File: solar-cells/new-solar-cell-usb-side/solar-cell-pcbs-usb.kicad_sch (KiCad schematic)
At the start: 22 parts, among them J1 Solar Cell

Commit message: bottom adapter plate sanity commit
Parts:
- removed H7: MountingHole_Pad, MountingHole:MountingHole_3.2mm_M3_DIN965_Pad, symbol Mechanical:MountingHole_Pad
- renumbered H8 to H7
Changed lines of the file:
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@@
     (pin "2")
-  )
-  (symbol (lib_id "power:GND") (at 48.26 138.43 0) (unit 1)
-    (in_bom yes) (on_board yes) (fields_autoplaced)
-    (property "Reference" "#PWR0108" (id 0) (at 48.26 144.78 0)
-      (effects (font (size 1.27 1.27)) hide)
-    )
-    (property "Value" "GND" (id 1) (at 48.26 143.51 0))
-    (property "Footprint" "" (id 2) (at 48.26 138.43 0)
-      (effects (font (size 1.27 1.27)) hide)
-    )
-    (property "Datasheet" "" (id 3) (at 48.26 138.43 0)
-      (effects (font (size 1.27 1.27)) hide)
-    )
-    (pin "1")
   )
   (symbol (lib_id "power:GND") (at 48.26 121.92 0) (unit 1)
@@
   (symbol (lib_id "Mechanical:MountingHole_Pad") (at 77.47 135.89 0) (unit 1)
     (in_bom yes) (on_board yes) (fields_autoplaced)
-    (property "Reference" "H8" (id 0) (at 80.01 133.3499 0)
+    (property "Reference" "H7" (id 0) (at 80.01 133.3499 0)
       (effects (font (size 1.27 1.27)) (justify left))
     )
@@
     (pin "2")
   )
-  (symbol (lib_id "Mechanical:MountingHole_Pad") (at 48.26 135.89 0) (unit 1)
-    (in_bom yes) (on_board yes)
-    (property "Reference" "H7" (id 0) (at 50.8 133.3499 0)
-      (effects (font (size 1.27 1.27)) (justify left))
-    )
-    (property "Value" "MountingHole_Pad" (id 1) (at 50.8 135.8899 0)
-      (effects (font (size 1.27 1.27)) (justify left))
-    )
-    (property "Footprint" "MountingHole:MountingHole_3.2mm_M3_DIN965_Pad" (id 2) (at 48.26 135.89 0)
-      (effects (font (size 1.27 1.27)) hide)
-    )
-    (property "Datasheet" "~" (id 3) (at 48.26 135.89 0)
-      (effects (font (size 1.27 1.27)) hide)
-    )
-    (pin "1")
-  )
   (symbol (lib_id "Device:Solar_Cell") (at 185.42 58.42 0) (unit 1)
     (in_bom yes) (on_board yes)
@@
       (reference "#PWR0107") (unit 1) (value "GND") (footprint "")
     )
-    (path "/5250df54-d711-4099-820d-6c1442819c3b"
-      (reference "#PWR0108") (unit 1) (value "GND") (footprint "")
-    )
     (path "/5fd6fd0b-b38c-4829-9eb3-2f584ac11f61"
       (reference "#PWR0109") (unit 1) (value "GND") (footprint "")
@@
       (reference "H6") (unit 1) (value "MountingHole_Pad") (footprint "MountingHole:MountingHole_3.2mm_M3_DIN965_Pad")
     )
-    (path "/ec72f6f6-dd1c-453c-aaba-004589220851"
+    (path "/a6717815-50da-423c-b99b-952ad2b012fb"
       (reference "H7") (unit 1) (value "MountingHole_Pad") (footprint "MountingHole:MountingHole_3.2mm_M3_DIN965_Pad")
     )
-    (path "/a6717815-50da-423c-b99b-952ad2b012fb"
-      (reference "H8") (unit 1) (value "MountingHole_Pad") (footprint "MountingHole:MountingHole_3.2mm_M3_DIN965_Pad")
-    )
     (path "/4d99938a-fe34-4ad4-80dd-a370c85df5e7"

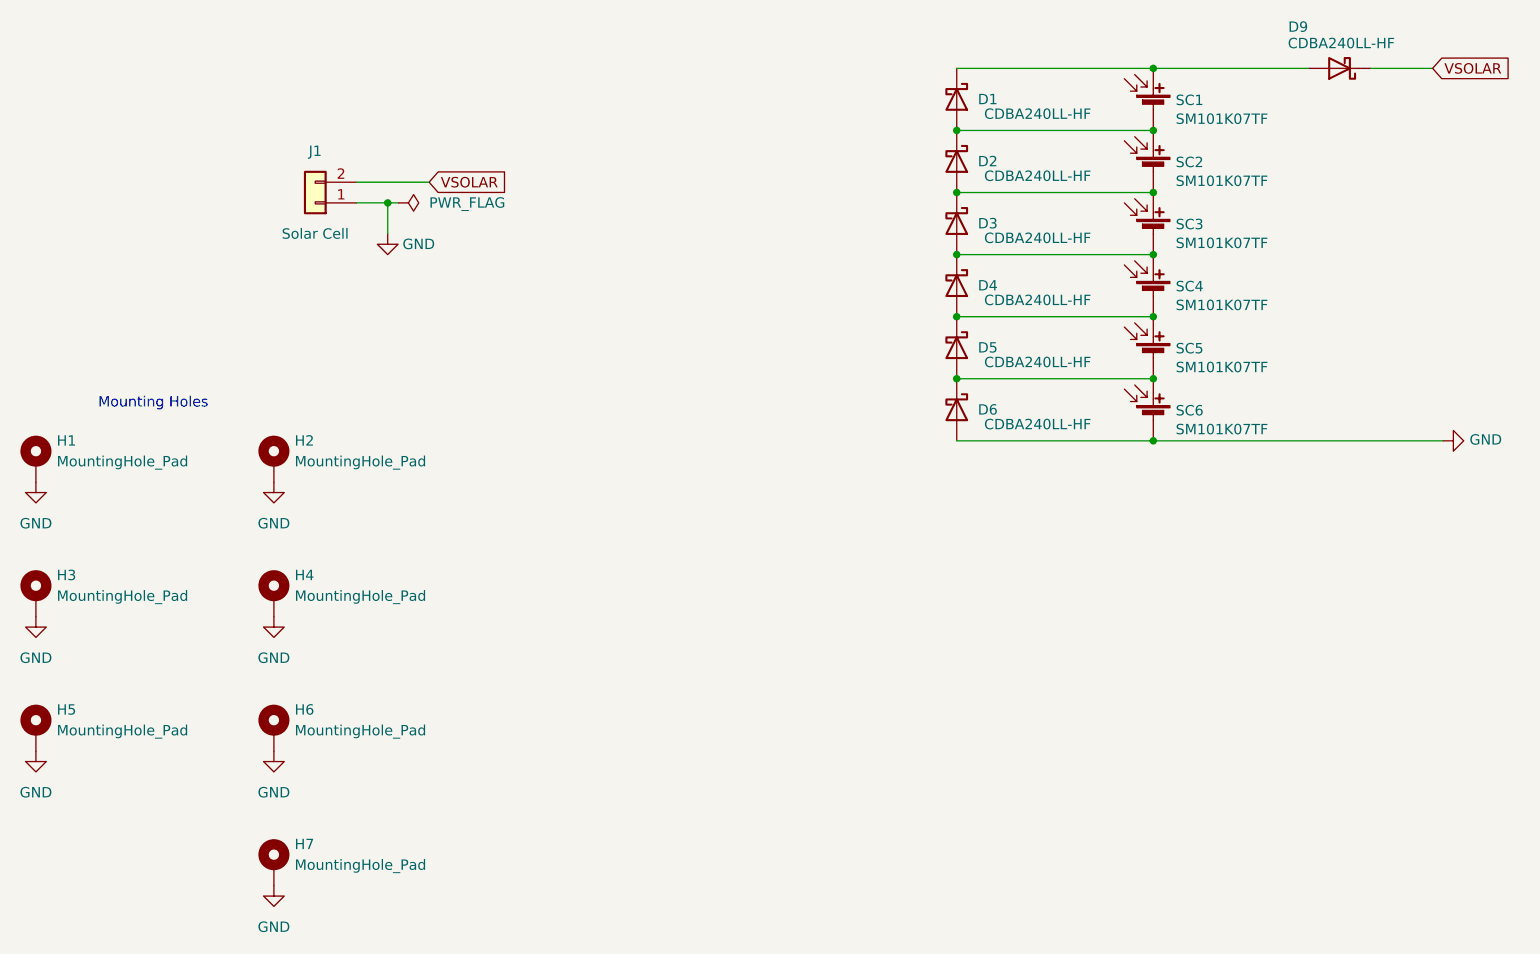
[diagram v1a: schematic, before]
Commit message: made solar cells 3s2p config
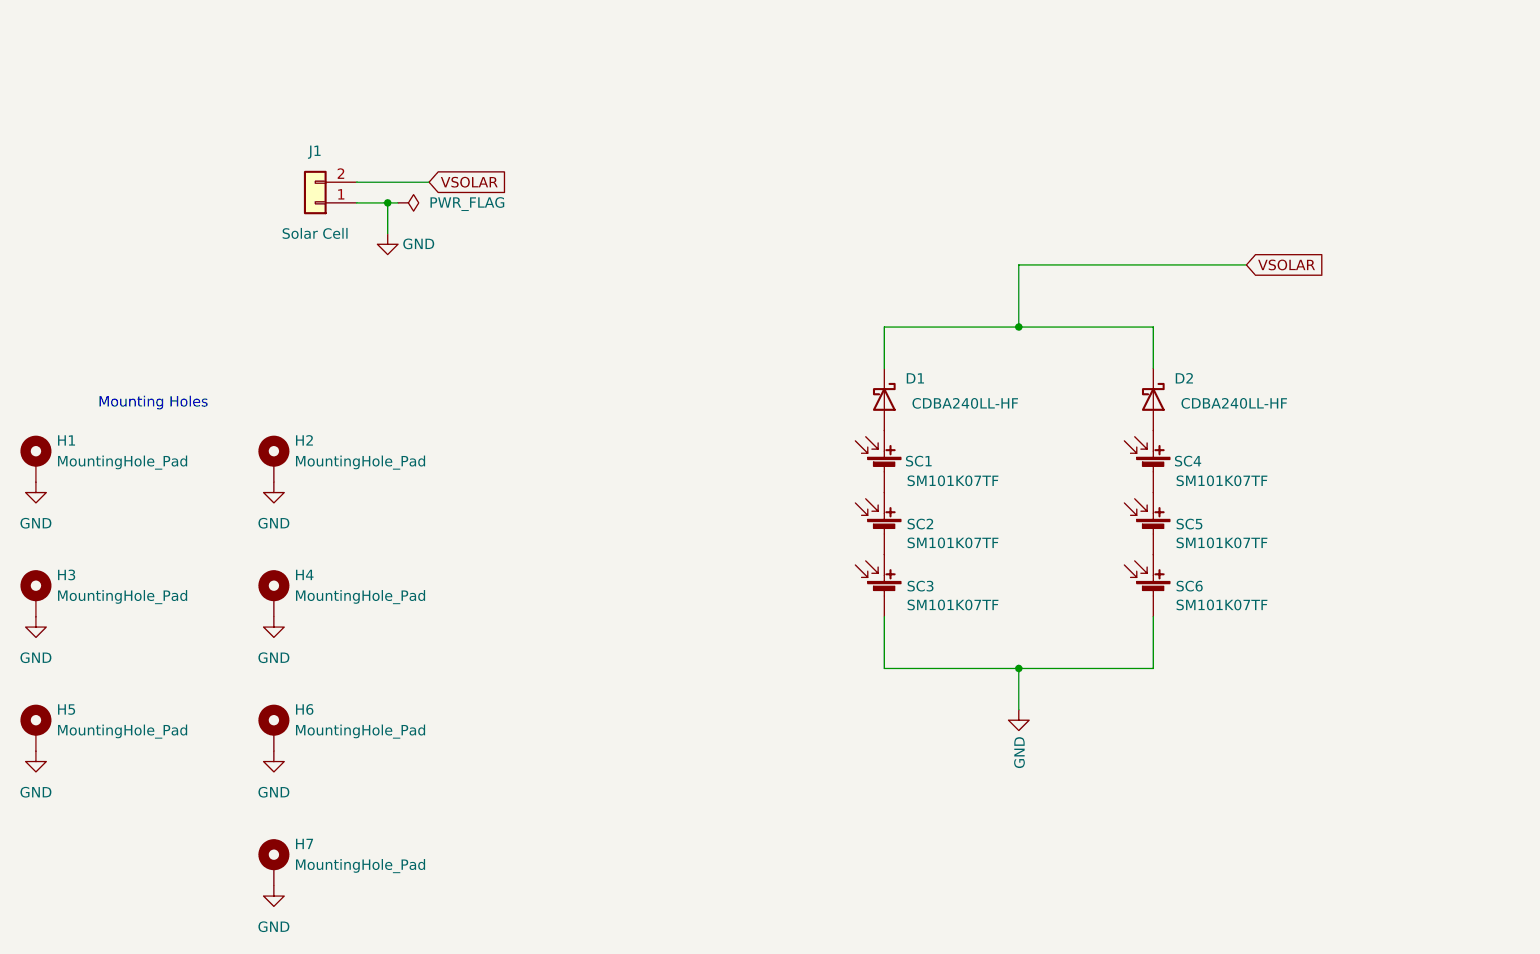
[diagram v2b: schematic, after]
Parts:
- removed D3, D4, D5, D6, D9: CDBA240LL-HF, ISP:DO-214AC, symbol Device:D_Schottky
- removed SC1, SC2, SC3: SM101K07TF, ISP:SM101K07TF, symbol Device:Solar_Cell
- added SC4, SC5, SC6: SM101K07TF, ISP:SM101K07TF, symbol Device:Solar_Cell
- renumbered SC4 to SC1, SC5 to SC2, SC6 to SC3
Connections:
- net GND: now also SC6.2 (-)
- net VSOLAR: now also D1.1 (K), D2.1 (K)
- net at D1.2 (A): now also SC1.1 (+); no longer D2.1 (K)
- net at D2.2 (A): now also SC4.1 (+)
- new net: SC4.2 (-), SC5.1 (+)
- new net: SC5.2 (-), SC6.1 (+)
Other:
- moved on the sheet: SC1, SC2, SC3
